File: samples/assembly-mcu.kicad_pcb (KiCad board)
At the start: 2 copper layers, 15.5 x 16.1 mm, 2 parts, among them J1 Conn_01x06_Pin

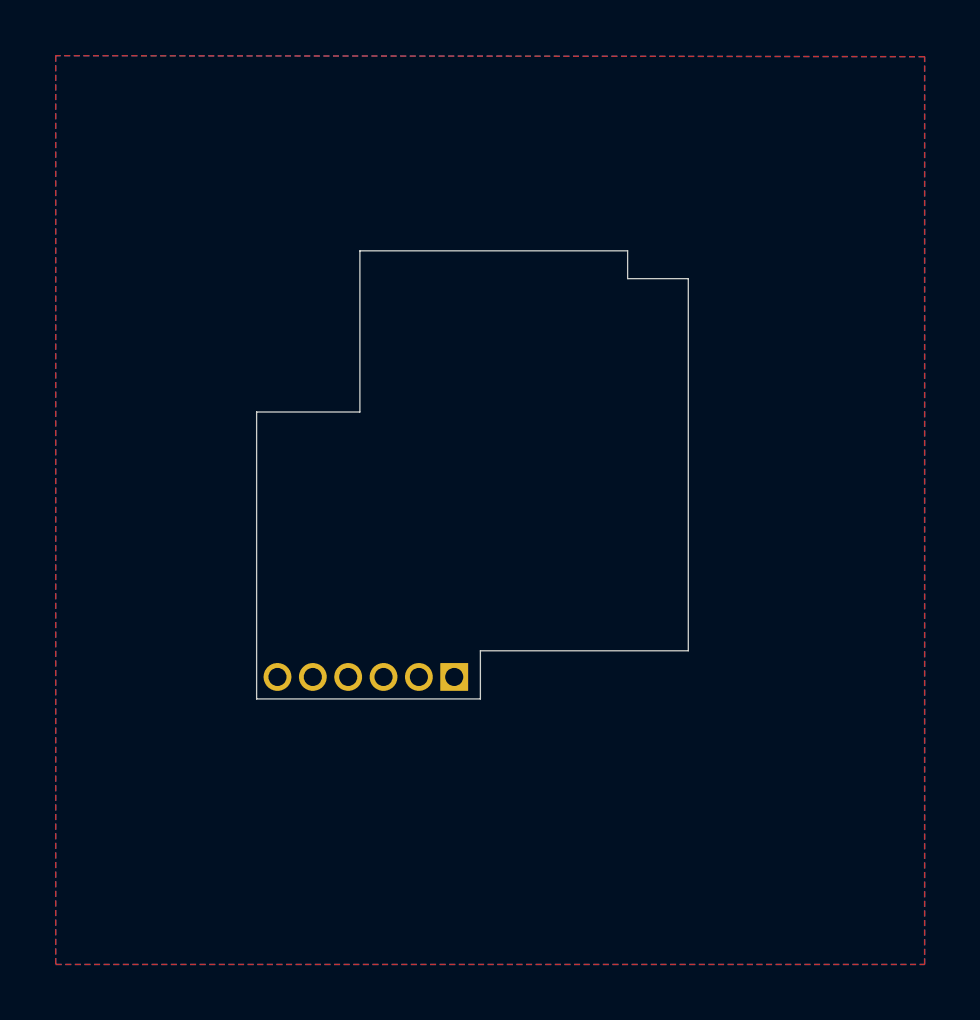
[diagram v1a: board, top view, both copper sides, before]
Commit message: Update assembly coupler samples
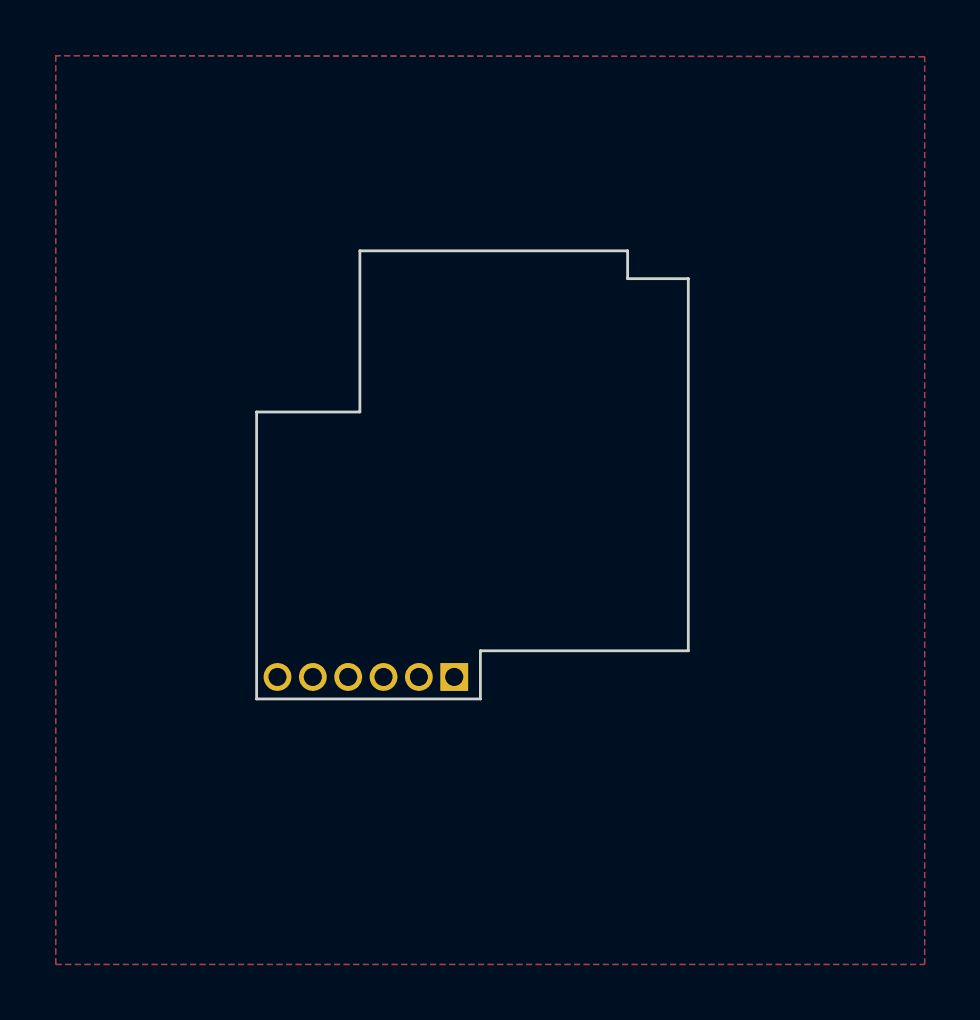
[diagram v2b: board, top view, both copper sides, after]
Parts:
- mcu: footprint Kikakuka:CouplerMoving -> PCM_Kikakuka:CouplerMoving
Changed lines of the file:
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@@
 		)
 	)
-	(footprint "Kikakuka:CouplerMoving"
+	(footprint "PCM_Kikakuka:CouplerMoving"
 		(layer "B.Cu")
 		(at 147.72 90 180)
@@
 			)
 		)
-		(property "Description" ""
+		(property "Description" "Moving FreekiCAD alignment plane. Positions this PCB against a CouplerFixed footprint with the same reference. Z moves along the PCB surface normal; positive Offset moves on the PCB surface in the triangle direction; Tilt rotates around local X. Unitless lengths default to mm; mm/in/mil/um are supported."
 			(at 0 0 0)
 			(unlocked yes)
@@
 			)
 		)
-		(property "Z" "1.1"
+		(property "Z" "1.1 mm"
 			(at 0 0 0)
 			(unlocked yes)
@@
 		)
 		(fp_line
+			(start 0.25 0.75)
+			(end 0 0.5)
+			(stroke
+				(width 0.1)
+				(type default)
+			)
+			(layer "Cmts.User")
+		)
+		(fp_line
+			(start 0 1)
+			(end 0 0.5)
+			(stroke
+				(width 0.1)
+				(type default)
+			)
+			(layer "Cmts.User")
+		)
+		(fp_line
+			(start 0 0.5)
+			(end -0.25 0.75)
+			(stroke
+				(width 0.1)
+				(type default)
+			)
+			(layer "Cmts.User")
+		)
+		(fp_line
 			(start 0 0)
 			(end -1 1)
+			(stroke
+				(width 0.1)
+				(type default)
+			)
+			(layer "Cmts.User")
+		)
+		(fp_line
+			(start -0.25 0.75)
+			(end 0 0.5)
 			(stroke
 				(width 0.1)
@@
 		(end 144.340599 82)
 		(stroke
-			(width 0)
+			(width 0.1)
 			(type default)
 		)
@@
 		(end 140.63 82)
 		(stroke
-			(width 0)
+			(width 0.1)
 			(type default)
 		)
@@
 		(end 153.96 76.21)
 		(stroke
-			(width 0)
+			(width 0.1)
 			(type default)
 		)
@@
 		(end 144.340599 76.21)
 		(stroke
-			(width 0)
+			(width 0.1)
 			(type default)
 		)
@@
 		(end 148.67 92.31)
 		(stroke
-			(width 0)
+			(width 0.1)
 			(type default)
 		)
@@
 		(end 140.63 92.31)
 		(stroke
-			(width 0)
+			(width 0.1)
 			(type default)
 		)
@@
 		(end 153.96 77.21)
 		(stroke
-			(width 0)
+			(width 0.1)
 			(type default)
 		)
@@
 		(end 156.14 77.21)
 		(stroke
-			(width 0)
+			(width 0.1)
 			(type default)
 		)
@@
 		(end 156.14 90.58)
 		(stroke
-			(width 0)
+			(width 0.1)
 			(type default)
 		)
@@
 		(end 148.67 90.58)
 		(stroke
-			(width 0)
+			(width 0.1)
 			(type default)
 		)
